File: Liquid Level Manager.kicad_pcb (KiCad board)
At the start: 2 copper layers, 12 parts, among them J1 +12V, Q1 IRLB8721PBF, U1 Full, U2 Low, U3 74LS02, U4 LM7805C

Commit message: wip
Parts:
- added J2: Valve, TerminalBlock:TerminalBlock_Altech_AK300-2_P5.00mm, F.Cu at (181.7, 118.1)
- added R2: 10k, Resistor_THT:R_Axial_DIN0516_L15.5mm_D5.0mm_P20.32mm_Horizontal, F.Cu at (119.4, 87.6)
- C1, C2: footprint Capacitor_THT:CP_Radial_D5.0mm_P2.00mm -> Capacitor_THT:CP_Radial_D5.0mm_P2.50mm
- R1: footprint Resistor_THT:R_Axial_DIN0204_L3.6mm_D1.6mm_P5.08mm_Horizontal -> Resistor_THT:R_Axial_DIN0516_L15.5mm_D5.0mm_P20.32mm_Horizontal
- U1: value Full -> High Sensor
- U2: value Low -> Low Sensor
- U3: footprint Package_DIP:DIP-14_W7.62mm_Socket -> Package_DIP:DIP-14_W7.62mm
- moved U4 72.1 mm to (148.6, 139.7)
- moved R1 69.3 mm to (119.4, 76.2), turned to 0 degrees
- moved C2 58.8 mm to (153.7, 132.1)
- moved C1 58.5 mm to (147.3, 130.8)
- moved J1 53.3 mm to (149.9, 118.1)
- moved U2 41.7 mm to (120.7, 130.8)
- moved D2 39.1 mm to (181.6, 91.4)
- moved D1 39.1 mm to (147.8, 94.4)
- moved D3 32.9 mm to (171.4, 102.9)
- moved U3 21.0 mm to (161.3, 73.7)
- moved U1 5.68 mm to (120.7, 113.0)
- moved Q1 5.08 mm to (199.4, 109.2)
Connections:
- D3 pad 1: Net-(D3-Pad1) -> +12V
- D3 pad 2: /VALVE -> Net-(D3-Pad2)
- Q1 pad 1: Net-(Q1-Pad1) -> /VALVE
- Q1 pad 2: Net-(Q1-Pad2) -> Net-(D3-Pad2)
- Q1 pad 3: Net-(Q1-Pad3) -> GND

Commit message: wip
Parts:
- R1, R2: footprint Resistor_THT:R_Axial_DIN0516_L15.5mm_D5.0mm_P20.32mm_Horizontal -> Resistor_THT:R_Axial_DIN0204_L3.6mm_D1.6mm_P5.08mm_Horizontal
- moved R1 64.2 mm to (176.5, 105.4), turned to 180 degrees
- moved J2 63.9 mm to (120.7, 99.1), turned to 270 degrees
- moved R2 58.3 mm to (176.5, 99.1), turned to 180 degrees
- moved U4 52.2 mm to (144.8, 87.6)
- moved U3 49.1 mm to (143.5, 119.4)
- moved J1 43.1 mm to (120.7, 86.4), turned to 270 degrees
- moved D2 43.0 mm to (167.6, 132.1), turned to 180 degrees
- moved C2 36.9 mm to (151.1, 95.2)
- moved C1 36.1 mm to (141.0, 95.2)
- moved Q1 35.3 mm to (171.4, 87.6)
- moved D1 33.9 mm to (167.6, 121.9), turned to 180 degrees
- moved D3 7.41 mm to (165.1, 99.1), turned to 270 degrees
- turned U1 to 270 degrees
- turned U2 to 270 degrees

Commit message: wip
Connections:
- net /VALVE renamed Net-(D1-Pad1)
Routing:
- net /5V: track 0.00 -> 91.9 mm
- net +12V: track 0.00 -> 82.4 mm
- net Net-(U2-Pad3): track 0.00 -> 34.1 mm
- net Net-(U1-Pad3): track 0.00 -> 26.5 mm
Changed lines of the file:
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@@
     (thickness 1.6)
     (drawings 0)
-    (tracks 0)
+    (tracks 40)
     (zones 0)
     (modules 14)
@@
   (net 6 +12V)
   (net 7 "Net-(U3-Pad1)")
-  (net 8 /VALVE)
-  (net 9 /5V)
-  (net 10 "Net-(D3-Pad2)")
+  (net 8 /5V)
+  (net 9 "Net-(D3-Pad2)")
+  (net 10 "Net-(D1-Pad1)")
   (net_class Default "This is the default net class."
     (clearance 0.2)
@@
     (add_net +12V)
     (add_net /5V)
-    (add_net /VALVE)
     (add_net GND)
+    (add_net "Net-(D1-Pad1)")
     (add_net "Net-(D1-Pad2)")
     (add_net "Net-(D2-Pad2)")
@@
       (net 2 GND))
     (pad 1 thru_hole rect (at 0 0) (size 1.6 1.6) (drill 0.8) (layers *.Cu *.Mask)
-      (net 9 /5V))
+      (net 8 /5V))
     (model ${KISYS3DMOD}/Capacitor_THT.3dshapes/CP_Radial_D5.0mm_P2.50mm.wrl
       (at (xyz 0 0 0))
@@
       (net 1 "Net-(D1-Pad2)"))
     (pad 1 thru_hole rect (at 0 0 180) (size 1.8 1.8) (drill 0.9) (layers *.Cu *.Mask)
-      (net 8 /VALVE))
+      (net 10 "Net-(D1-Pad1)"))
     (model ${KISYS3DMOD}/LED_THT.3dshapes/LED_D5.0mm.wrl
       (at (xyz 0 0 0))
@@
     )
     (pad 1 thru_hole rect (at 0 0 180) (size 1.8 1.8) (drill 0.9) (layers *.Cu *.Mask)
-      (net 8 /VALVE))
+      (net 10 "Net-(D1-Pad1)"))
     (pad 2 thru_hole circle (at 2.54 0 180) (size 1.8 1.8) (drill 0.9) (layers *.Cu *.Mask)
       (net 3 "Net-(D2-Pad2)"))
@@
       (net 6 +12V))
     (pad 2 thru_hole oval (at 10.16 0 270) (size 2.2 2.2) (drill 1.1) (layers *.Cu *.Mask)
-      (net 10 "Net-(D3-Pad2)"))
+      (net 9 "Net-(D3-Pad2)"))
     (model ${KISYS3DMOD}/Diode_THT.3dshapes/D_DO-41_SOD81_P10.16mm_Horizontal.wrl
       (at (xyz 0 0 0))
@@
     )
     (pad 2 thru_hole oval (at 5 0 270) (size 1.98 3.96) (drill 1.32) (layers *.Cu *.Mask)
-      (net 10 "Net-(D3-Pad2)"))
+      (net 9 "Net-(D3-Pad2)"))
     (pad 1 thru_hole rect (at 0 0 270) (size 1.98 3.96) (drill 1.32) (layers *.Cu *.Mask)
       (net 6 +12V))
@@
       (net 2 GND))
     (pad 2 thru_hole oval (at 2.54 0) (size 1.905 2) (drill 1.1) (layers *.Cu *.Mask)
-      (net 10 "Net-(D3-Pad2)"))
+      (net 9 "Net-(D3-Pad2)"))
     (pad 1 thru_hole rect (at 0 0) (size 1.905 2) (drill 1.1) (layers *.Cu *.Mask)
-      (net 8 /VALVE))
+      (net 10 "Net-(D1-Pad1)"))
     (model ${KISYS3DMOD}/Package_TO_SOT_THT.3dshapes/TO-220-3_Vertical.wrl
       (at (xyz 0 0 0))
@@
     (fp_arc (start -1.16 -4.66) (end -1.44 -4.14) (angle 104.2) (layer F.Fab) (width 0.1))
     (pad 1 thru_hole rect (at 0 0 270) (size 1.98 3.96) (drill 1.32) (layers *.Cu *.Mask)
-      (net 9 /5V))
+      (net 8 /5V))
     (pad 2 thru_hole oval (at 5 0 270) (size 1.98 3.96) (drill 1.32) (layers *.Cu *.Mask)
       (net 2 GND))
@@
       (net 2 GND))
     (pad 1 thru_hole rect (at 0 0 270) (size 1.98 3.96) (drill 1.32) (layers *.Cu *.Mask)
-      (net 9 /5V))
+      (net 8 /5V))
     (model ${KISYS3DMOD}/TerminalBlock.3dshapes/TerminalBlock_Altech_AK300-3_P5.00mm.wrl
       (at (xyz 0 0 0))
@@
       (net 2 GND))
     (pad 14 thru_hole oval (at 7.62 0) (size 1.6 1.6) (drill 0.8) (layers *.Cu *.Mask)
-      (net 9 /5V))
+      (net 8 /5V))
     (model ${KISYS3DMOD}/Package_DIP.3dshapes/DIP-14_W7.62mm.wrl
       (at (xyz 0 0 0))
@@
       (net 2 GND))
     (pad 3 thru_hole oval (at 5.08 0) (size 1.905 2) (drill 1.1) (layers *.Cu *.Mask)
-      (net 9 /5V))
+      (net 8 /5V))
     (model ${KISYS3DMOD}/Package_TO_SOT_THT.3dshapes/TO-220-3_Vertical.wrl
       (at (xyz 0 0 0))
@@
       (net 2 GND))
     (pad 2 thru_hole oval (at 5.08 0 180) (size 1.4 1.4) (drill 0.7) (layers *.Cu *.Mask)
-      (net 8 /VALVE))
+      (net 10 "Net-(D1-Pad1)"))
     (model ${KISYS3DMOD}/Resistor_THT.3dshapes/R_Axial_DIN0204_L3.6mm_D1.6mm_P5.08mm_Horizontal.wrl
       (at (xyz 0 0 0))
@@
     (fp_line (start 0.74 -0.8) (end 0.74 0.8) (layer F.Fab) (width 0.1))
     (pad 2 thru_hole oval (at 5.08 0 180) (size 1.4 1.4) (drill 0.7) (layers *.Cu *.Mask)
-      (net 8 /VALVE))
+      (net 10 "Net-(D1-Pad1)"))
     (pad 1 thru_hole circle (at 0 0 180) (size 1.4 1.4) (drill 0.7) (layers *.Cu *.Mask)
       (net 2 GND))
@@
     )
   )
+  (segment (start 142.4 123.03) (end 143.51 121.92) (width 0.25) (layer F.Cu) (net 4))
+  (segment (start 142.08 123.03) (end 143.51 124.46) (width 0.25) (layer F.Cu) (net 4))
+  (segment (start 140.97 123.03) (end 142.08 123.03) (width 0.25) (layer F.Cu) (net 4))
+  (segment (start 140.97 123.03) (end 142.4 123.03) (width 0.25) (layer F.Cu) (net 4))
+  (segment (start 120.65 123.03) (end 140.97 123.03) (width 0.25) (layer F.Cu) (net 4))
+  (segment (start 142.4 140.81) (end 151.13 132.08) (width 0.25) (layer F.Cu) (net 5))
+  (segment (start 120.65 140.81) (end 142.4 140.81) (width 0.25) (layer F.Cu) (net 5))
+  (segment (start 144.78 87.5825) (end 144.78 87.63) (width 0.25) (layer F.Cu) (net 6))
+  (segment (start 143.5575 86.36) (end 144.78 87.5825) (width 0.25) (layer F.Cu) (net 6))
+  (segment (start 140.97 92.71) (end 134.62 86.36) (width 0.25) (layer F.Cu) (net 6))
+  (segment (start 140.97 95.25) (end 140.97 92.71) (width 0.25) (layer F.Cu) (net 6))
+  (segment (start 133.35 87.35) (end 133.35 86.36) (width 0.25) (layer F.Cu) (net 6))
+  (segment (start 121.64 99.06) (end 133.35 87.35) (width 0.25) (layer F.Cu) (net 6))
+  (segment (start 120.65 99.06) (end 121.64 99.06) (width 0.25) (layer F.Cu) (net 6))
+  (segment (start 120.65 86.36) (end 133.35 86.36) (width 0.25) (layer F.Cu) (net 6))
+  (segment (start 133.35 86.36) (end 134.62 86.36) (width 0.25) (layer F.Cu) (net 6))
+  (segment (start 143.56501 86.30499) (end 143.51 86.36) (width 0.25) (layer F.Cu) (net 6))
+  (segment (start 153.69499 86.30499) (end 143.56501 86.30499) (width 0.25) (layer F.Cu) (net 6))
+  (segment (start 165.1 97.71) (end 153.69499 86.30499) (width 0.25) (layer F.Cu) (net 6))
+  (segment (start 165.1 99.06) (end 165.1 97.71) (width 0.25) (layer F.Cu) (net 6))
+  (segment (start 134.62 86.36) (end 143.51 86.36) (width 0.25) (layer F.Cu) (net 6))
+  (segment (start 143.51 86.36) (end 143.5575 86.36) (width 0.25) (layer F.Cu) (net 6))
+  (segment (start 150.08 95.25) (end 151.13 95.25) (width 0.25) (layer F.Cu) (net 8))
+  (segment (start 149.86 95.03) (end 150.08 95.25) (width 0.25) (layer F.Cu) (net 8))
+  (segment (start 149.86 87.63) (end 149.86 95.03) (width 0.25) (layer F.Cu) (net 8))
+  (segment (start 151.13 95.25) (end 151.13 109.22) (width 0.25) (layer F.Cu) (net 8))
+  (segment (start 151.13 109.22) (end 151.13 119.38) (width 0.25) (layer F.Cu) (net 8))
+  (segment (start 120.65 113.03) (end 121.64 113.03) (width 0.25) (layer F.Cu) (net 8))
+  (segment (start 149.86 107.95) (end 151.13 109.22) (width 0.25) (layer F.Cu) (net 8))
+  (segment (start 137.16 107.95) (end 149.86 107.95) (width 0.25) (layer F.Cu) (net 8))
+  (segment (start 126.72 107.95) (end 137.16 107.95) (width 0.25) (layer F.Cu) (net 8))
+  (segment (start 122.184694 119.34501) (end 125.45 116.079704) (width 0.25) (layer F.Cu) (net 8))
+  (segment (start 125.45 116.079704) (end 125.45 109.22) (width 0.25) (layer F.Cu) (net 8))
+  (segment (start 121.485286 119.34501) (end 122.184694 119.34501) (width 0.25) (layer F.Cu) (net 8))
+  (segment (start 118.34499 122.485306) (end 121.485286 119.34501) (width 0.25) (layer F.Cu) (net 8))
+  (segment (start 118.34499 127.26499) (end 118.34499 122.485306) (width 0.25) (layer F.Cu) (net 8))
+  (segment (start 120.65 130.81) (end 120.65 129.57) (width 0.25) (layer F.Cu) (net 8))
+  (segment (start 120.65 129.57) (end 118.34499 127.26499) (width 0.25) (layer F.Cu) (net 8))
+  (segment (start 125.45 109.22) (end 126.72 107.95) (width 0.25) (layer F.Cu) (net 8))
+  (segment (start 121.64 113.03) (end 125.45 109.22) (width 0.25) (layer F.Cu) (net 8))
 )

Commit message: wip
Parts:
- added C3: .1uF, Capacitor_THT:C_Disc_D5.1mm_W3.2mm_P5.00mm, F.Cu at (138.4, 54.6)
- added REF**: M2, MountingHole:MountingHole_2.2mm_M2, F.Cu at (103.4, 49.8)
- added REF**: M2, MountingHole:MountingHole_2.2mm_M2, F.Cu at (178.8, 49.3)
- added REF**: M2, MountingHole:MountingHole_2.2mm_M2, F.Cu at (103.9, 117.6)
- added REF**: M2, MountingHole:MountingHole_2.2mm_M2, F.Cu at (178.1, 117.9)
- J1, J2: footprint TerminalBlock:TerminalBlock_Altech_AK300-2_P5.00mm -> TerminalBlock_4Ucon:TerminalBlock_4Ucon_1x02_P3.50mm_Horizontal
- R1, R2: footprint Resistor_THT:R_Axial_DIN0204_L3.6mm_D1.6mm_P5.08mm_Horizontal -> Resistor_THT:R_Axial_DIN0207_L6.3mm_D2.5mm_P7.62mm_Horizontal
- U1, U2: footprint TerminalBlock:TerminalBlock_Altech_AK300-3_P5.00mm -> TerminalBlock_4Ucon:TerminalBlock_4Ucon_1x03_P3.50mm_Horizontal
- moved U3 63.3 mm to (145.5, 56.1), turned to 90 degrees
- moved D2 54.4 mm to (173.6, 78.0), turned to 0 degrees
- moved U2 41.2 mm to (158.5, 114.6), turned to 0 degrees
- moved Q1 40.4 mm to (131.6, 94.2)
- moved U4 38.0 mm to (113.3, 66.3)
- moved C2 37.2 mm to (120.1, 74.7), turned to 90 degrees
- moved C1 36.1 mm to (111.3, 74.7), turned to 90 degrees
- moved D3 35.8 mm to (129.3, 99.6), turned to 0 degrees
- moved R2 32.8 mm to (143.8, 99.6), turned to 90 degrees
- moved D1 32.3 mm to (173.6, 90.2), turned to 0 degrees
- moved J1 28.2 mm to (121.2, 114.6), turned to 0 degrees
- moved U1 24.9 mm to (145.5, 114.6), turned to 0 degrees
- moved R1 20.5 mm to (166.4, 87.6), turned to 90 degrees
- moved J2 19.3 mm to (132.1, 114.6), turned to 0 degrees
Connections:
- U3 pad 14: /5V -> Net-(C3-Pad1)
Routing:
- net /5V: track 91.9 -> 0.00 mm
- net +12V: track 82.4 -> 0.00 mm
- net Net-(U2-Pad3): track 34.1 -> 0.00 mm
- net Net-(U1-Pad3): track 26.5 -> 0.00 mm
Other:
- board outline added: 89.2 x 82 mm

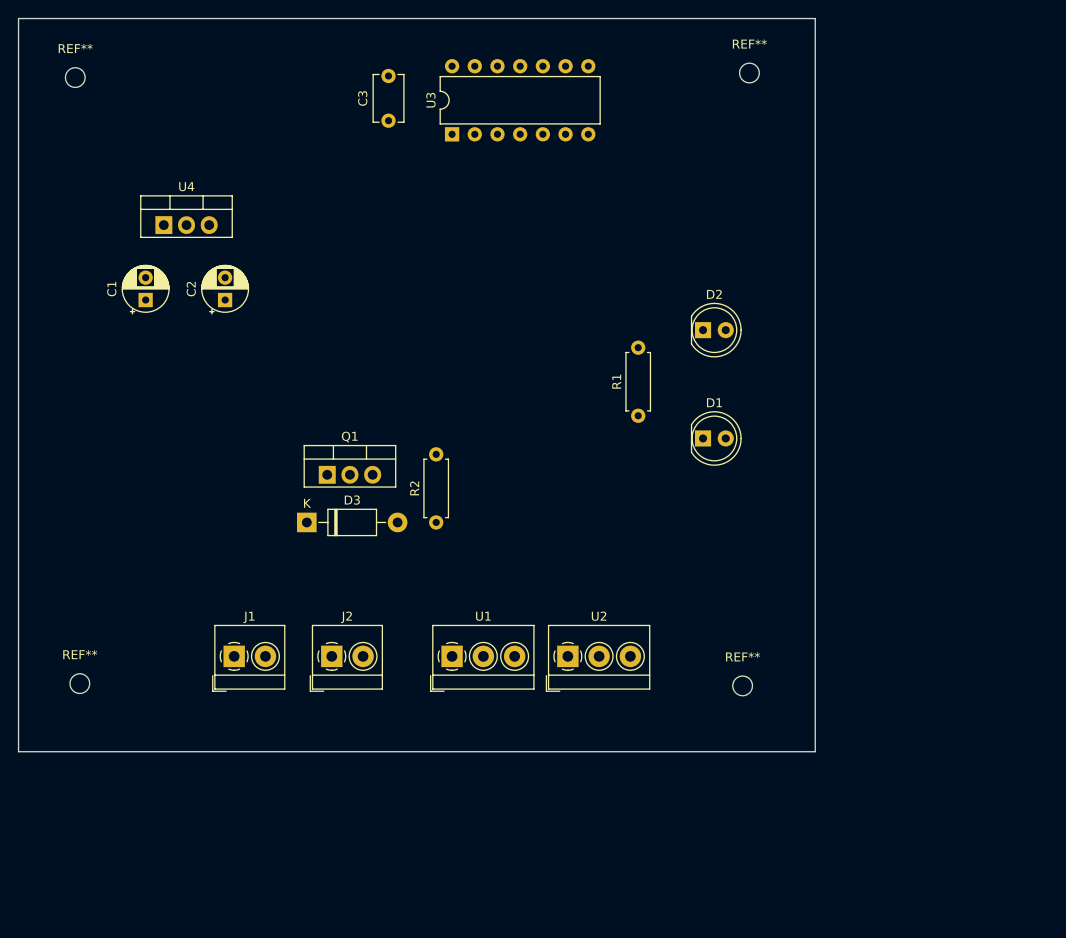
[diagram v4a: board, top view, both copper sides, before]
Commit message: small schema change and pcb tweaks
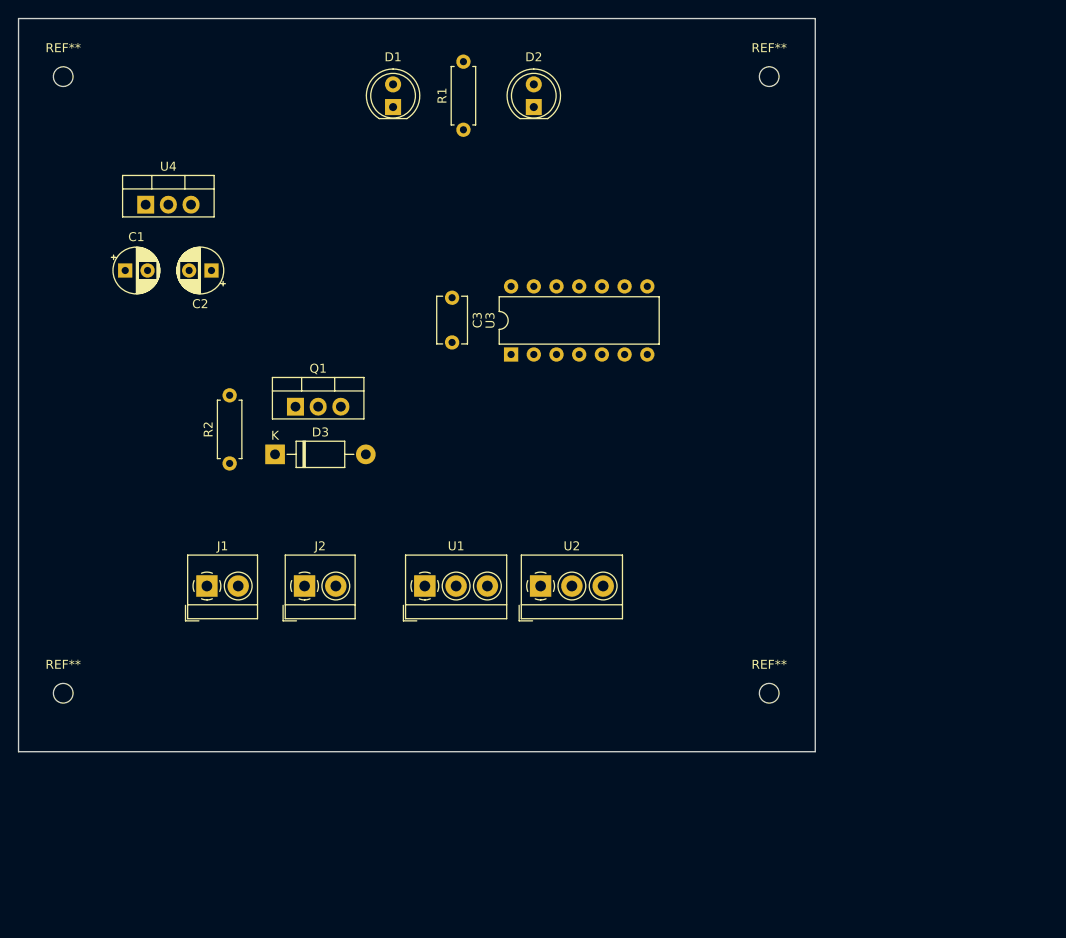
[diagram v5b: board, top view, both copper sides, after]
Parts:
- moved D1 50.8 mm to (138.9, 53.1), turned to 90 degrees
- moved R1 37.5 mm to (146.8, 55.6)
- moved D2 31.3 mm to (154.7, 53.1), turned to 90 degrees
- moved U3 25.5 mm to (152.1, 80.8)
- moved R2 24.0 mm to (120.7, 93.0)
- moved C3 21.0 mm to (145.5, 74.4), turned to 270 degrees
- moved J1 8.44 mm to (118.1, 106.7)
- moved J2 8.44 mm to (129.0, 106.7)
- moved U1 8.44 mm to (142.5, 106.7)
- moved U2 8.44 mm to (155.4, 106.7)
- moved D3 8.41 mm to (125.7, 91.9)
- moved Q1 8.41 mm to (128.0, 86.6)
- moved C1 4.02 mm to (109.0, 71.4), turned to 0 degrees
- moved C2 3.64 mm to (118.6, 71.4), turned to 180 degrees
- moved REF** 3.09 mm to (181.0, 118.7)
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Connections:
- D2 pad 2: Net-(D2-Pad2) -> /VALVE
- Q1 pad 1: Net-(D1-Pad1) -> /VALVE
- R2 pad 2: Net-(D1-Pad1) -> /VALVE
- U3 pad 4: Net-(D2-Pad2) -> /VALVE
- U3 pad 8: Net-(D2-Pad2) -> /VALVE

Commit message: cleaned up the schematic, working on pcb
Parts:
- removed J2: Valve, TerminalBlock_4Ucon:TerminalBlock_4Ucon_1x02_P3.50mm_Horizontal
- added J3: +12V, TerminalBlock_4Ucon:TerminalBlock_4Ucon_1x02_P3.50mm_Horizontal, F.Cu at (117.3, 106.2)
- J1: value +12V -> Valve
- moved D1 13.5 mm to (149.1, 62.0)
- moved R1 13.5 mm to (157.0, 64.5)
- moved D2 13.5 mm to (164.8, 62.0)
- moved J1 11.7 mm to (129.8, 106.2)
- moved C3 6.35 mm to (145.5, 80.8)
- moved U3 6.35 mm to (152.1, 87.1)
- moved U2 3.84 mm to (159.3, 106.2)
- moved U1 2.84 mm to (145.3, 106.2)
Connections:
- net /5V renamed +5V
- net /VALVE renamed SENSOR_OUT
- J1 pad 1: +12V -> Net-(D3-Pad2)
- J1 pad 2: GND -> +12V
